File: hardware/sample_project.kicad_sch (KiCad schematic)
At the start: 3 parts

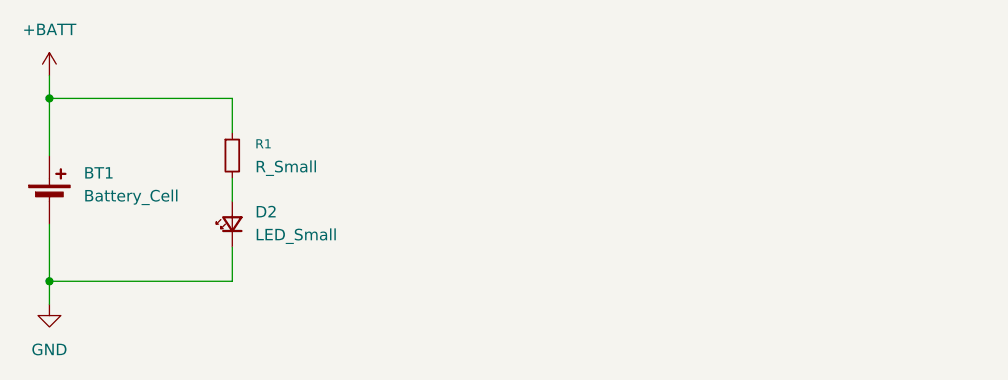
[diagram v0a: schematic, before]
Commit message: added positions and 3D model
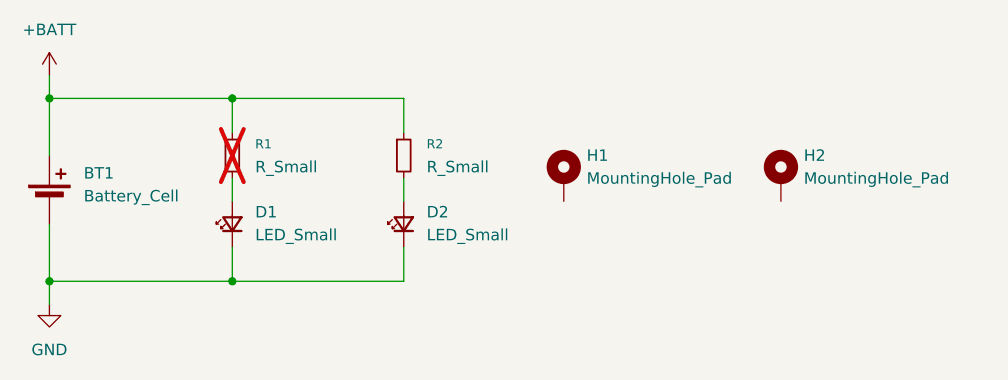
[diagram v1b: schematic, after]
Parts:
- added D1: LED_Small, LED_SMD:LED_0805_2012Metric, symbol Device:LED_Small
- added H1, H2: MountingHole_Pad, MountingHole:MountingHole_3.2mm_M3_Pad_Via, symbol Mechanical:MountingHole_Pad
- added R2: R_Small, Resistor_THT:R_Axial_DIN0207_L6.3mm_D2.5mm_P10.16mm_Horizontal, symbol Device:R_Small
- D2: footprint LED_SMD:LED_0805_2012Metric -> LED_THT:LED_D3.0mm
- R1: now not fitted
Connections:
- net +BATT: now also R2.1
- net GND: now also D1.1 (K)
- net at R1.2: now also D1.2 (A); no longer D2.2 (A)
- new net: D2.2 (A), R2.2
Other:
- moved on the sheet: D2
